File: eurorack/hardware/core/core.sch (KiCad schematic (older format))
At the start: 50 parts, among them J1 ConnNW, J2 ConnSW, J3 ConnNE, J4 ConnSE, J5 Power, J6 SWD, SW1 Reset, SW2 Boot0, U1 STM32F427VGT6, U2 TLV320AIC23BPW, U3 LM1117F-3.3, U4 LM4040C10IDBZR, Y1 Crystal

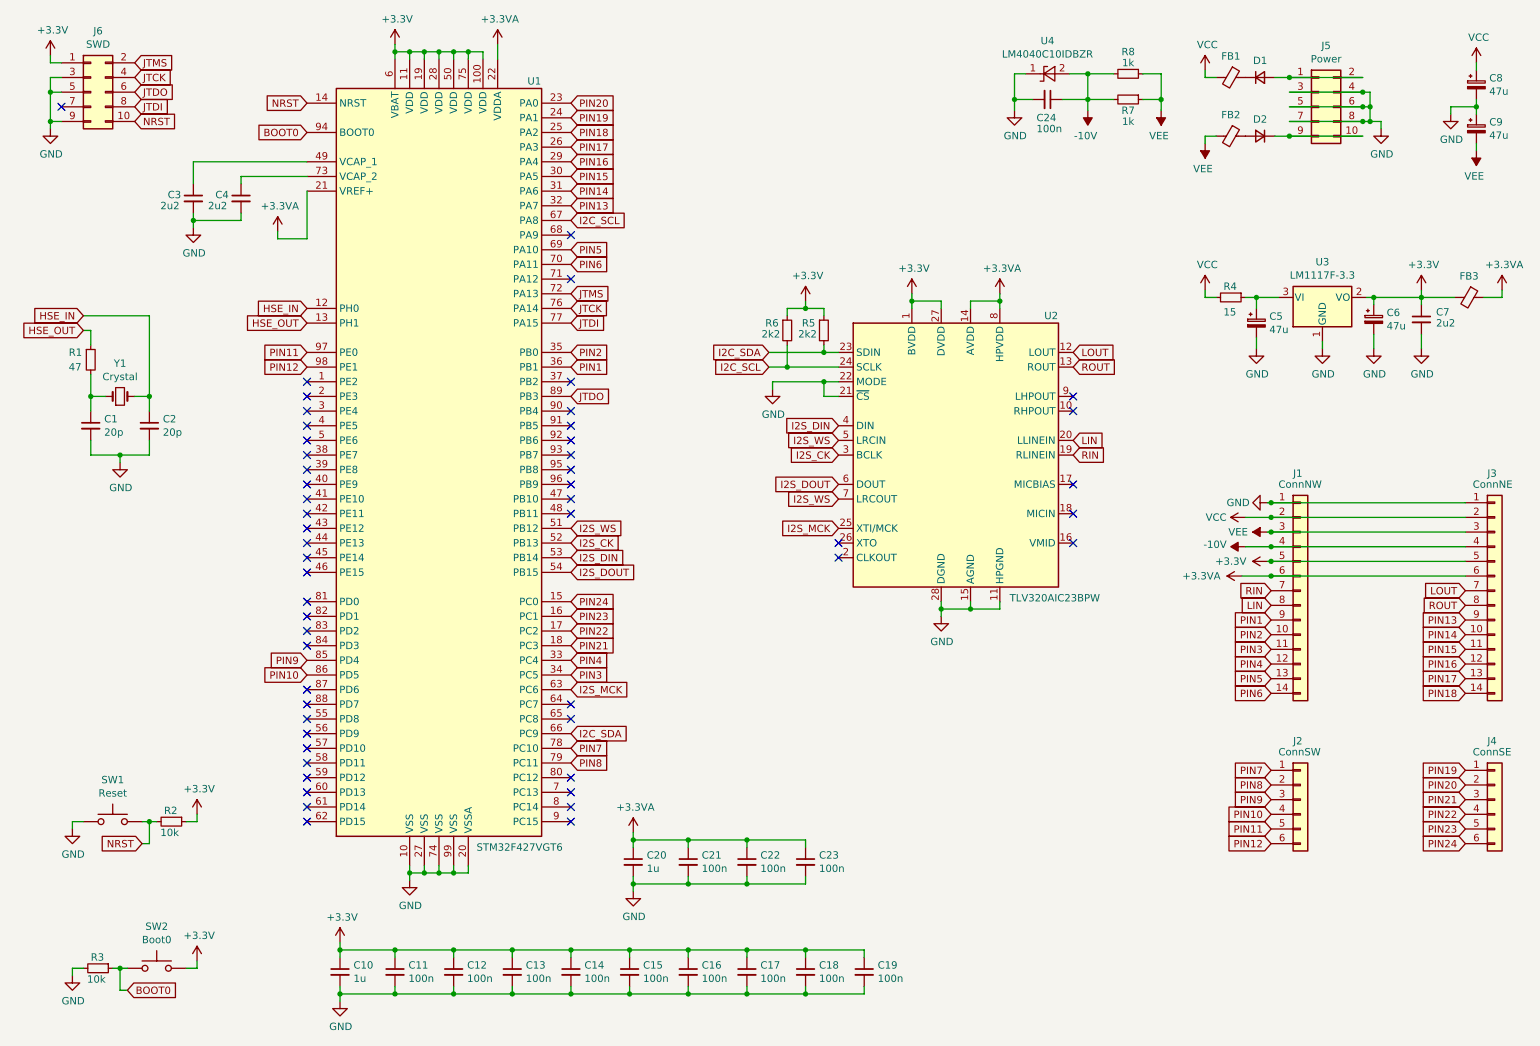
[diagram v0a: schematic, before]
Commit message: Switch to STM32H743VIT6
It is twice the price of STM32F4 on JLCPCB and twice as fast.

Signed-off-by: Petr Horacek <hrck@protonmail.com>
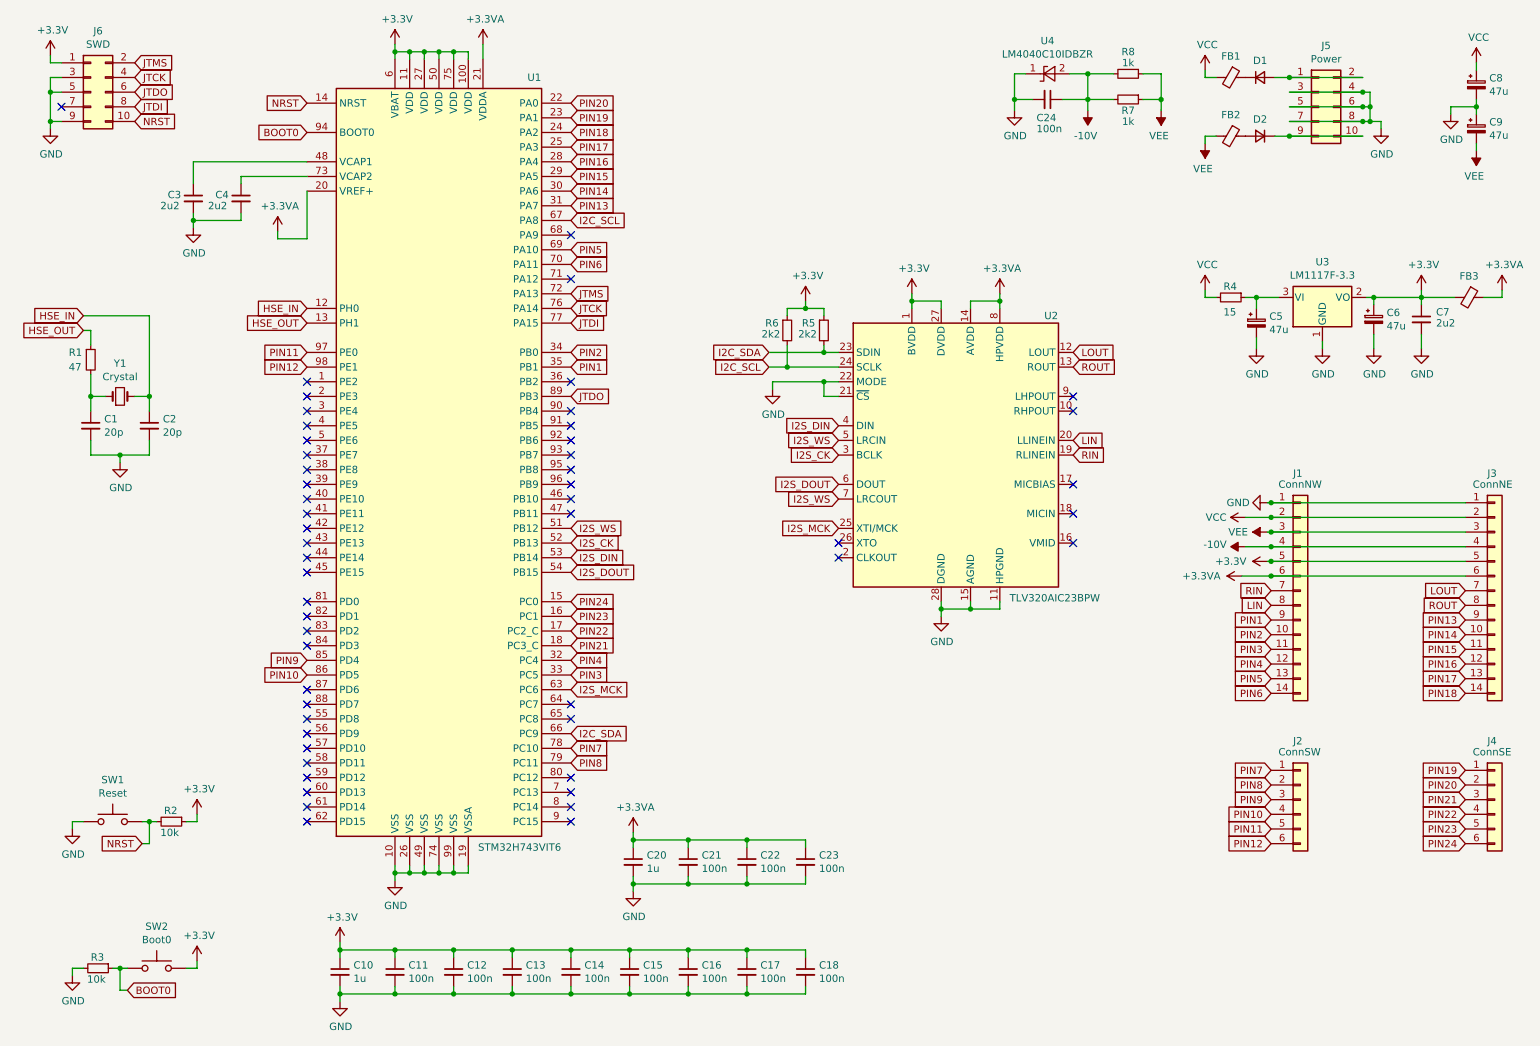
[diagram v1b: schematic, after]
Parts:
- removed C19: 100n, Capacitor_SMD:C_0402_1005Metric, symbol Device:C_Small
- removed U1: STM32F427VGT6, Package_QFP:LQFP-100_14x14mm_P0.5mm, symbol MCU_ST_STM32F4:STM32F427VGTx
- added U1: STM32H743VIT6, Package_QFP:LQFP-100_14x14mm_P0.5mm, symbol MCU_ST_STM32H7:STM32H743VITx
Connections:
- net +3.3VA: now also U1.20 (VREF+), U1.21 (VDDA)
- net +3V3: now also U1.100 (VDD), U1.11 (VDD), U1.27 (VDD), U1.50 (VDD), U1.6 (VBAT), U1.75 (VDD)
- net BOOT0: now also U1.94 (BOOT0)
- net GND: now also U1.10 (VSS), U1.19 (VSSA), U1.26 (VSS), U1.49 (VSS), U1.74 (VSS), U1.99 (VSS)
- net HSE_IN: now also U1.12 (PH0)
- net HSE_OUT: now also U1.13 (PH1)
- net I2C_SCL: now also U1.67 (PA8)
- net I2C_SDA: now also U1.66 (PC9)
- net I2S_CK: now also U1.52 (PB13)
- net I2S_DIN: now also U1.53 (PB14)
- net I2S_DOUT: now also U1.54 (PB15)
- net I2S_MCK: now also U1.63 (PC6)
- net I2S_WS: now also U1.51 (PB12)
- net JTCK: now also U1.76 (PA14)
- net JTDI: now also U1.77 (PA15)
- net JTDO: now also U1.89 (PB3)
- net JTMS: now also U1.72 (PA13)
- net NRST: now also U1.14 (NRST)
- net PIN1: now also U1.35 (PB1)
- net PIN10: now also U1.86 (PD5)
- net PIN11: now also U1.97 (PE0)
- net PIN12: now also U1.98 (PE1)
- net PIN13: now also U1.31 (PA7)
- net PIN14: now also U1.30 (PA6)
- net PIN15: now also U1.29 (PA5)
- net PIN16: now also U1.28 (PA4)
- net PIN17: now also U1.25 (PA3)
- net PIN18: now also U1.24 (PA2)
- net PIN19: now also U1.23 (PA1)
- net PIN2: now also U1.34 (PB0)
- net PIN20: now also U1.22 (PA0)
- net PIN21: now also U1.18 (PC3_C)
- net PIN22: now also U1.17 (PC2_C)
- net PIN23: now also U1.16 (PC1)
- net PIN24: now also U1.15 (PC0)
- net PIN3: now also U1.33 (PC5)
- net PIN4: now also U1.32 (PC4)
- net PIN5: now also U1.69 (PA10)
- net PIN6: now also U1.70 (PA11)
- net PIN7: now also U1.78 (PC10)
- net PIN8: now also U1.79 (PC11)
- net PIN9: now also U1.85 (PD4)
- net at C3.1: now also U1.48 (VCAP1)
- net at C4.1: now also U1.73 (VCAP2)
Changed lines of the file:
@@
 $EndDescr
-$Comp
-L MCU_ST_STM32F4:STM32F427VGTx U1
-U 1 1 60870DB2
-P 3550 3650
-F 0 "U1" H 4200 6200 50  0000 C CNN
-F 1 " STM32F427VGT6" H 4100 975 50  0000 C CNN
-F 2 "Package_QFP:LQFP-100_14x14mm_P0.5mm" H 2850 1050 50  0001 R CNN
-F 3 "http://www.st.com/st-web-ui/static/active/en/resource/technical/document/datasheet/DM00071990.pdf" H 3550 3650 50  0001 C CNN
-F 4 "C117815" H 3550 3650 50  0001 C CNN "LCSC Part #"
-F 5 "C117815" H 3550 3650 50  0001 C CNN "LCSC"
-	1    3550 3650
-	1    0    0    -1
-$EndComp
 $Comp
 L Audio:TLV320AIC23BPW U2
@@
 L power:+3.3VA #PWR03
 U 1 1 60B878C3
-P 3950 850
-F 0 "#PWR03" H 3950 700 50  0001 C CNN
-F 1 "+3.3VA" H 3965 1023 50  0000 C CNN
-F 2 "" H 3950 850 50  0001 C CNN
-F 3 "" H 3950 850 50  0001 C CNN
-	1    3950 850
-	1    0    0    -1
-$EndComp
-Wire Wire Line
-	3950 950  3950 850
+P 3850 850
+F 0 "#PWR03" H 3850 700 50  0001 C CNN
+F 1 "+3.3VA" H 3865 1023 50  0000 C CNN
+F 2 "" H 3850 850 50  0001 C CNN
+F 3 "" H 3850 850 50  0001 C CNN
+	1    3850 850
+	1    0    0    -1
+$EndComp
+Wire Wire Line
+	3850 950  3850 850
 $Comp
 L power:+3.3VA #PWR02
@@
 Wire Wire Line
 	3250 900  3350 900
-Wire Wire Line
-	3850 900  3850 950
 Connection ~ 3250 900
 Wire Wire Line
@@
 Wire Wire Line
 	3750 950  3750 900
-Connection ~ 3750 900
-Wire Wire Line
-	3750 900  3850 900
 Wire Wire Line
 	3650 950  3650 900
@@
 L power:GND #PWR0102
 U 1 1 60BB4C61
-P 3350 6550
-F 0 "#PWR0102" H 3350 6300 50  0001 C CNN
-F 1 "GND" H 3355 6377 50  0000 C CNN
-F 2 "" H 3350 6550 50  0001 C CNN
-F 3 "" H 3350 6550 50  0001 C CNN
-	1    3350 6550
+P 3250 6550
+F 0 "#PWR0102" H 3250 6300 50  0001 C CNN
+F 1 "GND" H 3255 6377 50  0000 C CNN
+F 2 "" H 3250 6550 50  0001 C CNN
+F 3 "" H 3250 6550 50  0001 C CNN
+	1    3250 6550
 	1    0    0    -1
 $EndComp
@@
 Wire Wire Line
 	3750 6500 3750 6450
-Connection ~ 3350 6500
-Wire Wire Line
-	3350 6500 3350 6550
 Wire Wire Line
 	3650 6450 3650 6500
@@
 	1    0    0    -1
 $EndComp
-$Comp
-L Device:C_Small C19
-U 1 1 60F6EE39
-P 6450 7175
-F 0 "C19" H 6542 7221 50  0000 L CNN
-F 1 "100n" H 6542 7130 50  0000 L CNN
-F 2 "Capacitor_SMD:C_0402_1005Metric" H 6450 7175 50  0001 C CNN
-F 3 "~" H 6450 7175 50  0001 C CNN
-F 4 "C1525" H 6450 7175 50  0001 C CNN "LCSC Part #"
-F 5 "C1525" H 6450 7175 50  0001 C CNN "LCSC"
-	1    6450 7175
-	1    0    0    -1
-$EndComp
 Wire Wire Line
 	5650 7025 6050 7025
@@
 	6050 7025 6050 7075
 Wire Wire Line
-	6050 7025 6450 7025
-Wire Wire Line
-	6450 7025 6450 7075
-Connection ~ 6050 7025
-Wire Wire Line
 	5650 7325 6050 7325
 Wire Wire Line
 	6050 7325 6050 7275
-Wire Wire Line
-	6450 7325 6450 7275
-Wire Wire Line
-	6050 7325 6450 7325
-Connection ~ 6050 7325
 Connection ~ 5650 7025
 Connection ~ 5650 7325
@@
 	6175 2950 6175 2900
 Wire Wire Line
-	6275 3050 5925 3050
-Wire Wire Line
 	5925 3050 5925 2900
 $Comp
@@
 	5925 2650 5925 2700
 Wire Wire Line
-	6050 2650 6175 2650
-Wire Wire Line
 	6175 2650 6175 2700
 Connection ~ 6050 2650
-Wire Wire Line
-	6175 2950 5800 2950
 Connection ~ 6175 2950
 Wire Wire Line
@@
 Wire Wire Line
 	5825 3150 5825 3200
-Wire Wire Line
-	5825 3150 6175 3150
 Text GLabel 4450 4350 2    50   Input ~ 0
 I2S_DIN
@@
 NoConn ~ 4450 6150
 NoConn ~ 7875 4250
+$Comp
+L MCU_ST_STM32H7:STM32H743VITx U1
+U 1 1 6240D4B7
+P 3550 3650
+F 0 "U1" H 4200 6225 50  0000 C CNN
+F 1 "STM32H743VIT6" H 4100 975 50  0000 C CNN
+F 2 "Package_QFP:LQFP-100_14x14mm_P0.5mm" H 2850 1050 50  0001 R CNN
+F 3 "http://www.st.com/st-web-ui/static/active/en/resource/technical/document/datasheet/DM00387108.pdf" H 3550 3650 50  0001 C CNN
+F 4 "C114409" H 3550 3650 50  0001 C CNN "LCSC"
+F 5 "C114409" H 3550 3650 50  0001 C CNN "LCSC Part #"
+	1    3550 3650
+	1    0    0    -1
+$EndComp
+Wire Wire Line
+	5825 3150 6175 3150
+Wire Wire Line
+	5925 3050 6275 3050
+Wire Wire Line
+	5800 2950 6175 2950
+Wire Wire Line
+	6050 2650 6175 2650
+Wire Wire Line
+	3250 6450 3250 6500
+Wire Wire Line
+	3350 6500 3250 6500
+Connection ~ 3350 6500
+Connection ~ 3250 6500
+Wire Wire Line
+	3250 6500 3250 6550
 $EndSCHEMATC
